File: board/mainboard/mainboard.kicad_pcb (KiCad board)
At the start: 2 copper layers, 148.1 x 58.4 mm, 97 parts, among them P1 I2C, P10 BUMPERS, P12 POWER, P2 MOTOR 1, P3 MOTOR 2, P4 SPI, P5 DAC, P6 LINE SENSORS, P7 ANALOG, P8 OPTIONAL PERIPHERALS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

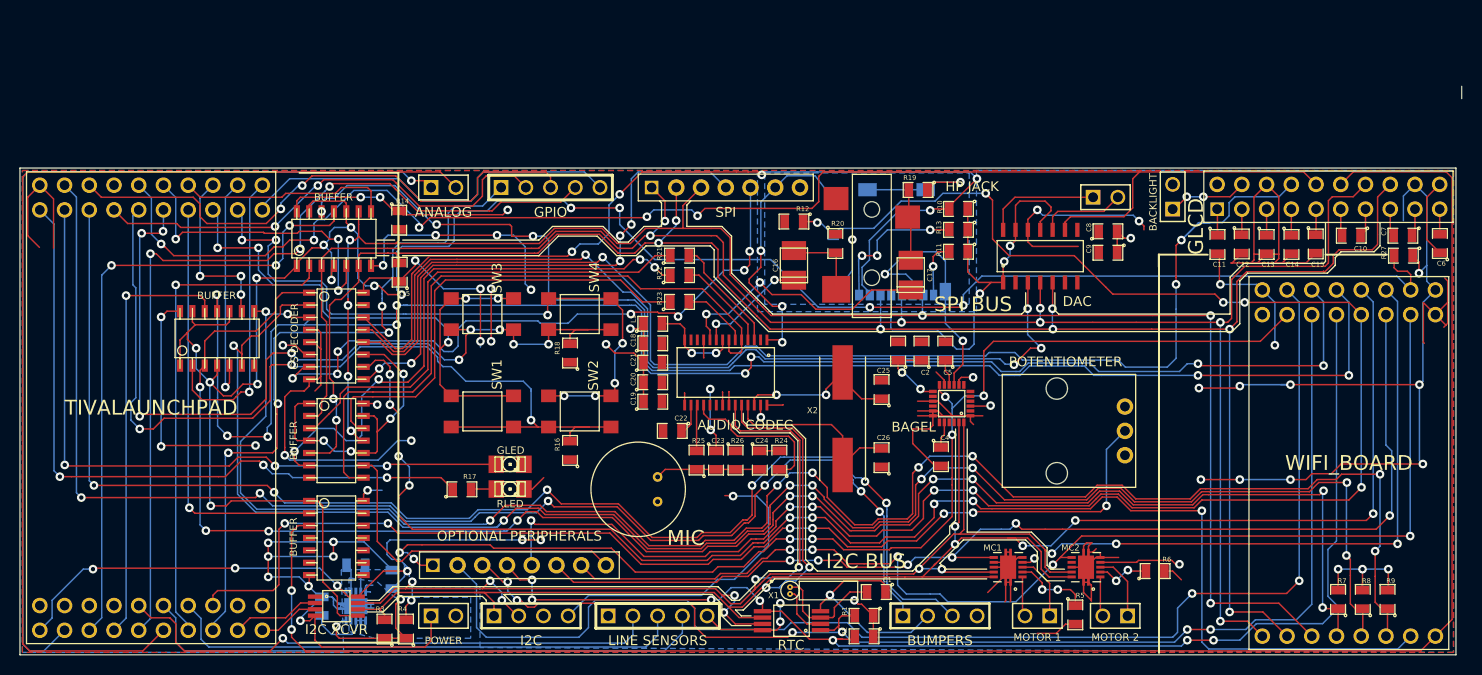
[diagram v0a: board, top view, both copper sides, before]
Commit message: Fixed busses to be same width
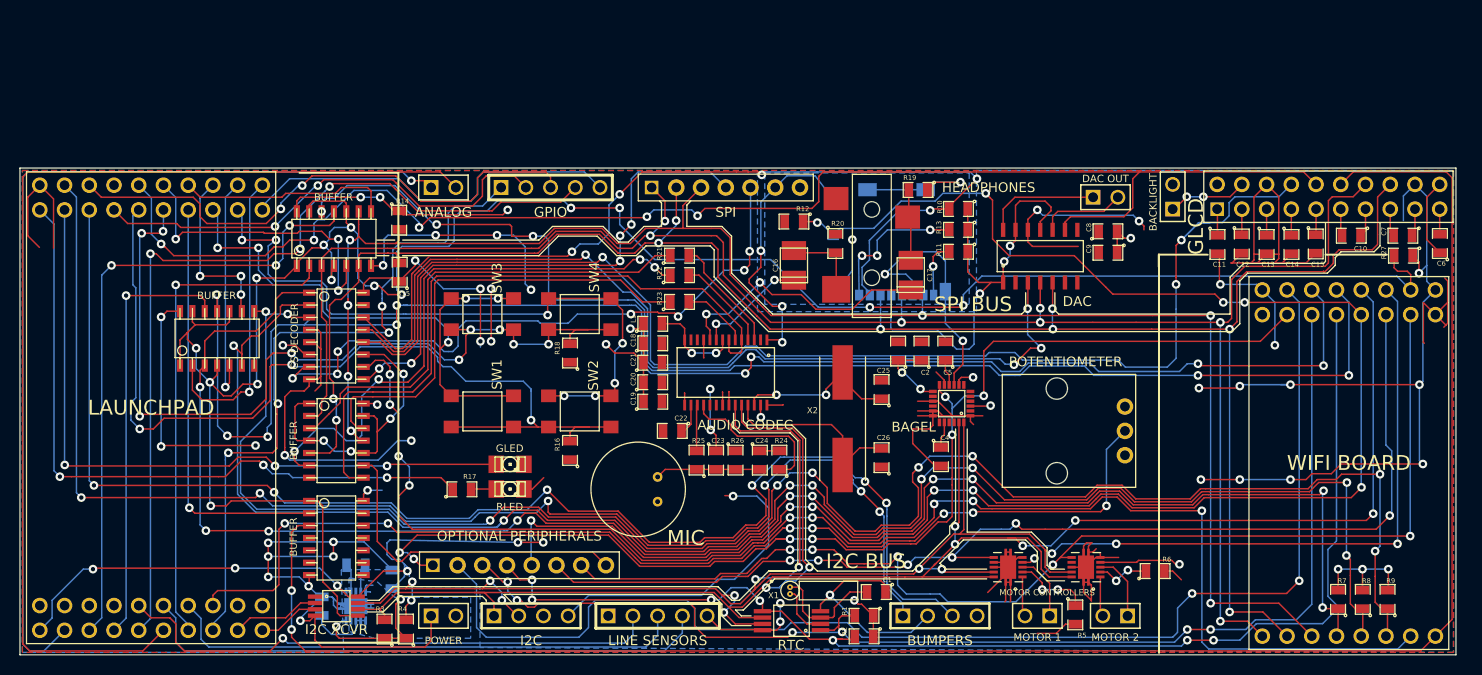
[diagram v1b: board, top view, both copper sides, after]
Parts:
- DAC OUT: renamed from P5
- HP1: value HP JACK -> HEADPHONES
- LP1: value TIVALAUNCHPAD -> LAUNCHPAD
- MOTOR CONTROLLERS: renamed from MC1
- WB1: value WIFI_BOARD -> WIFI BOARD
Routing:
- net BUMP2: track 138.1 -> 140.5 mm
- net BUMP1: track 137.6 -> 139.9 mm
- net SPI_SEL2: track 181.1 -> 183.1 mm
- net MPUINT: track 120.6 -> 122.4 mm
- net SPI_SEL1: track 177.0 -> 178.5 mm
- net SPI_SEL0: track 178.2 -> 179.5 mm
- net SD_SWITCH: track 186.3 -> 187.1 mm
- net POT: track 113.5 -> 114.2 mm
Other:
- board size 148.1 x 58.4 mm -> 147.5 x 50 mm
- board text added: "Proxima Rev 1.1"

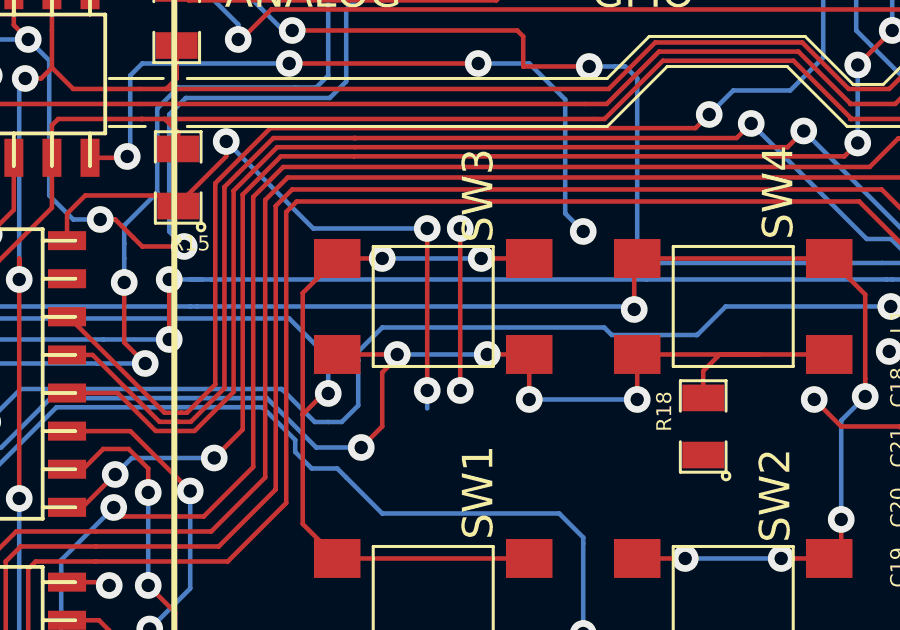
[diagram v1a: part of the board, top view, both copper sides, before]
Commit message: Fixed bug with an unconnected net
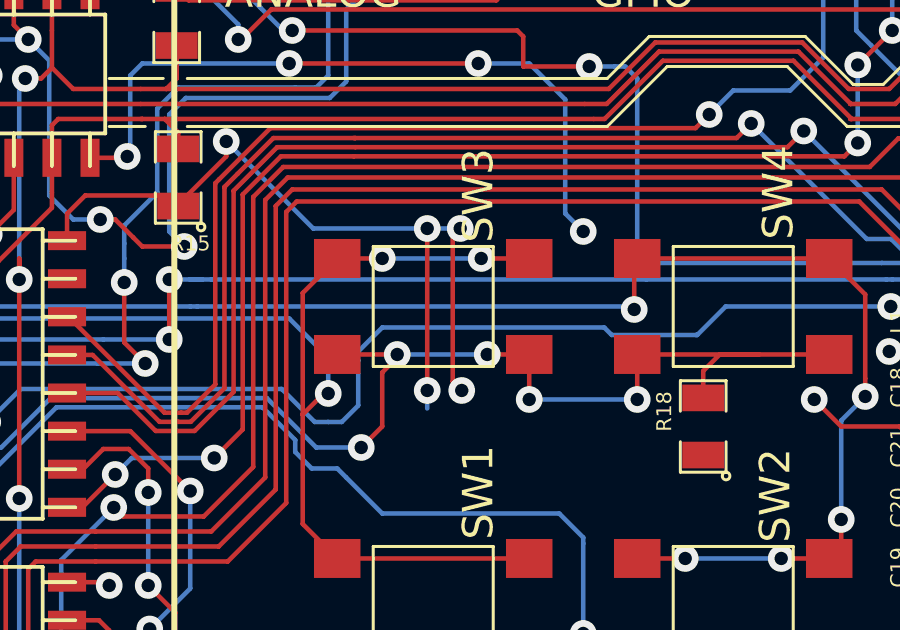
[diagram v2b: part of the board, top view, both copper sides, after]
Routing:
- net 3V3: track 377.8 -> 384.6 mm, vias 48 -> 50
- net (no net): track 5.40 -> 0.00 mm, vias 2 -> 0
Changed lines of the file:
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@@
     (thickness 1.6)
     (drawings 125)
-    (tracks 2750)
+    (tracks 2753)
     (zones 0)
     (modules 97)
@@
   (gr_line (start 156.21 158.75) (end 166.37 158.75) (angle 90) (layer F.SilkS) (width 0.2))
   (gr_line (start 244.475 118.885) (end 244.475 120.155) (angle 90) (layer F.SilkS) (width 0.2))
-  (via (at 175.9 127.8) (size 0.889) (layers F.Cu B.Cu) (net 0))
-  (via (at 175.9 122.4) (size 0.889) (layers F.Cu B.Cu) (net 0))
-  (segment (start 175.9 127.8) (end 175.9 122.4) (width 0.1524) (layer F.Cu) (net 0))
+  (segment (start 174.8 122.4) (end 175.9 122.4) (width 0.1524) (layer B.Cu) (net 1))
+  (via (at 175.95 127.8) (size 0.889) (layers F.Cu B.Cu) (net 1))
+  (segment (start 175.65 127.5) (end 175.95 127.8) (width 0.1524) (layer F.Cu) (net 1))
+  (segment (start 175.65 122.65) (end 175.65 127.5) (width 0.1524) (layer F.Cu) (net 1))
+  (segment (start 175.9 122.4) (end 175.65 122.65) (width 0.1524) (layer F.Cu) (net 1))
+  (via (at 175.9 122.4) (size 0.889) (layers F.Cu B.Cu) (net 1))
   (segment (start 129.54 157.48) (end 130.8 156.22) (width 0.1524) (layer B.Cu) (net 1))
   (segment (start 158.3 151.1) (end 160.1 152.9) (width 0.1524) (layer B.Cu) (net 1))

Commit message: Added Penguin Skywalker
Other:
- board text added: "Proxima Rev 1.1 Penguin Skywalker"
- board text removed: "Proxima Rev 1.1"
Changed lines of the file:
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@@
     (pad_to_mask_clearance 0)
     (aux_axis_origin 0 0)
-    (visible_elements 7FFFFBBF)
+    (visible_elements 7FFFFBAF)
     (pcbplotparams
       (layerselection 284196865)
@@
     )
   )
-  (gr_text "Proxima\nRev 1.1" (at 183.8 137.45) (layer B.SilkS)
-    (effects (font (size 2 2) (thickness 0.3)) (justify mirror))
+  (gr_text "Proxima\nRev 1.1\nPenguin Skywalker" (at 197.4 132.55) (layer B.SilkS)
+    (effects (font (size 2 2) (thickness 0.3)) (justify left mirror))
   )
   (gr_text "SPI BUS" (at 248.8 127.8 90) (layer B.SilkS)

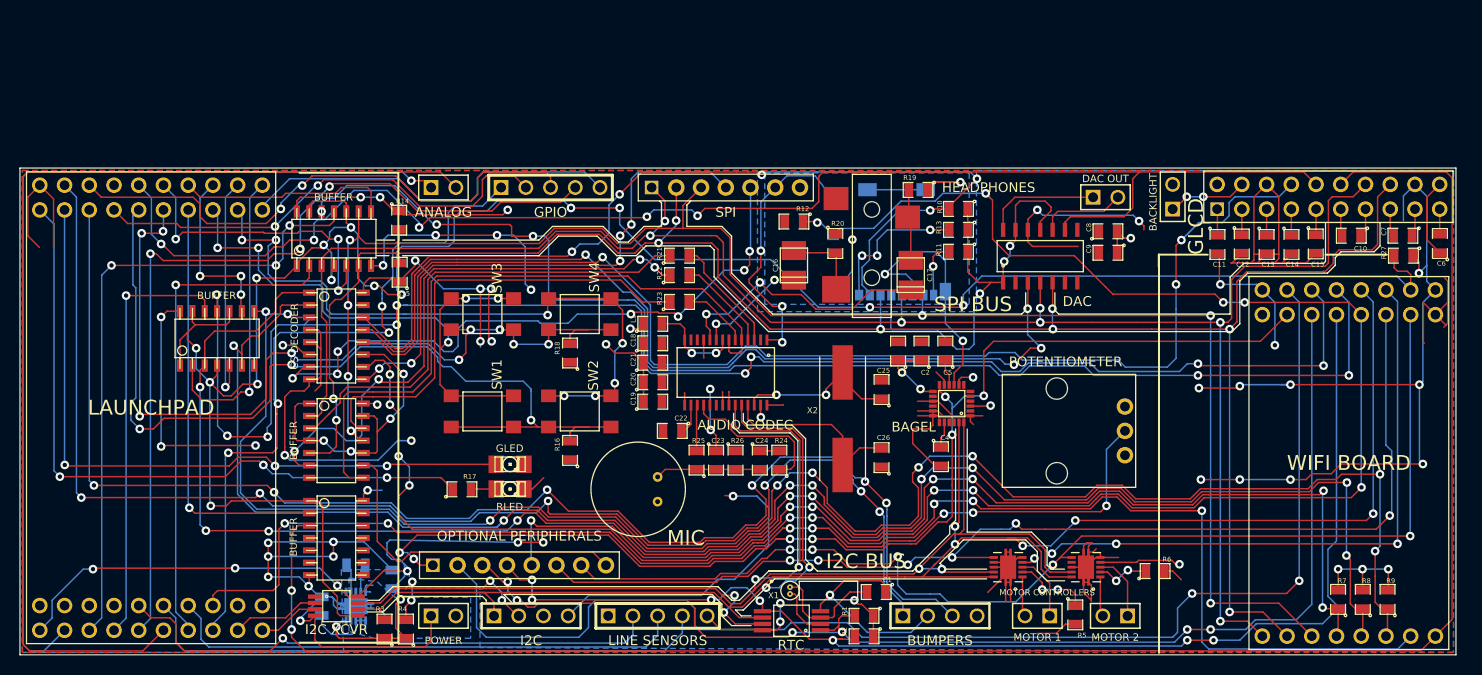
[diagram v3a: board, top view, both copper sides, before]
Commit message: Fixed layout issues with mainboard v1.1
* Increased width of power traces
* Increased number of traces connecting power and ground planes
* Cleaned up some routing
* Reduced via size
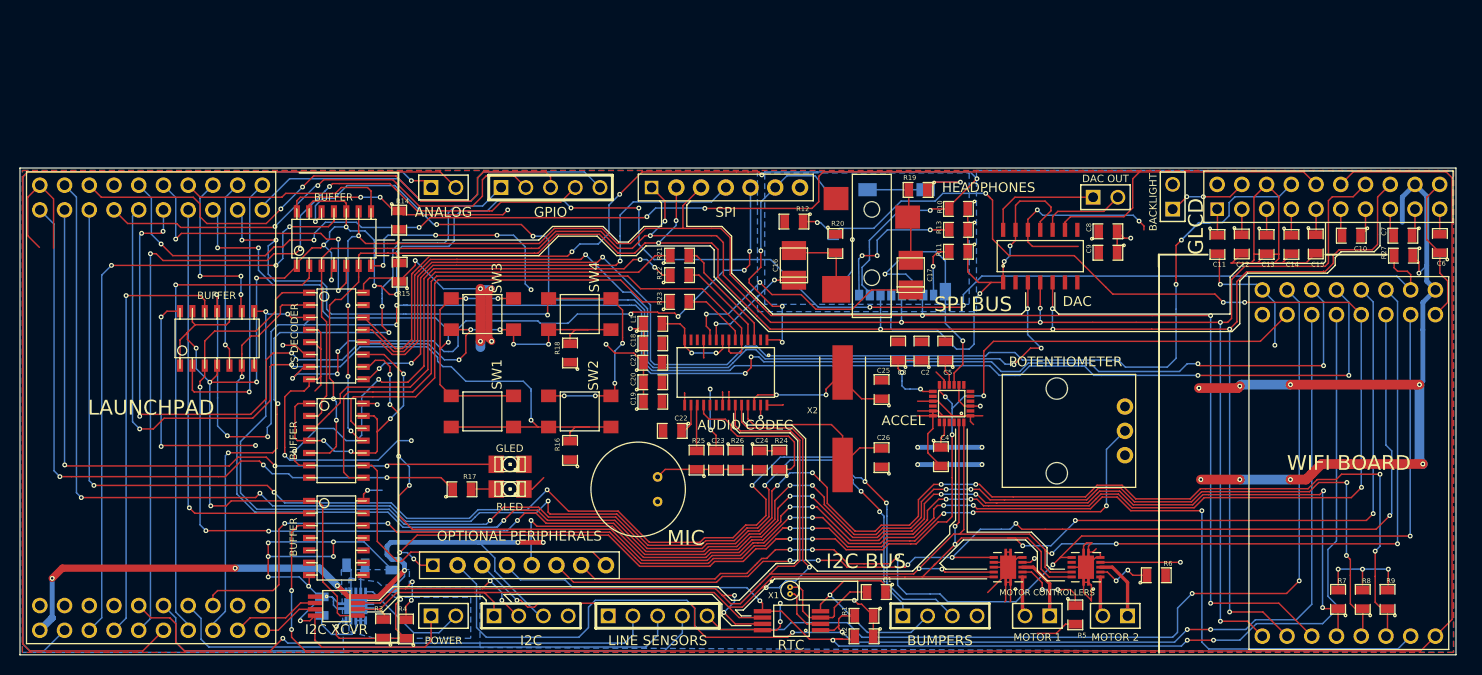
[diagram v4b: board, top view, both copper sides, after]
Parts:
- MPU1: value BAGEL -> ACCEL
- moved R6 0.45 mm to (244.2, 151.8)
- moved R3 0.16 mm to (164.8, 157.3)
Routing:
- net GND: track 430.7 -> 385.5 mm, vias 28 -> 27
- net (no net): track 0.00 -> 13.2 mm, vias 0 -> 4
- net 3V3: track 384.6 -> 395.9 mm, vias 50 -> 49
- net N-00000121: track 10.9 -> 18.8 mm
- net SPI_SEL1: track 178.5 -> 172.2 mm
- net SPI_SEL2: track 183.1 -> 178.2 mm
- net SPI_SEL1_LP: track 23.6 -> 19.2 mm
- net RST: track 149.0 -> 144.9 mm
- net I2C_DA: track 211.0 -> 207.5 mm, vias 13 -> 11
- net SPI_CS6: track 55.6 -> 52.7 mm, vias 5 -> 3
- net RTCINT2: track 127.4 -> 125.1 mm, vias 7 -> 4
- net SPI_SEL0: track 179.5 -> 177.4 mm
- net UART_RX: track 132.8 -> 135.0 mm
- net SD_SWITCH: track 187.1 -> 185.6 mm
- net CC_CONTROL: track 235.8 -> 234.8 mm
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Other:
- net class Default: via_dia 0.889 -> 0.5; via_drill 0.635 -> 0.3
- rule via_min_drill: 0.508 -> 0.3
- rule via_min_size: 0.889 -> 0.5
- board text added: "Crayon Dinosaur RN, DS, HV"
- board text added: "Proxima Rev 1.2"
- board text removed: "Proxima Rev 1.1 Penguin Skywalker"

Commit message: Removed audio codec from layout.
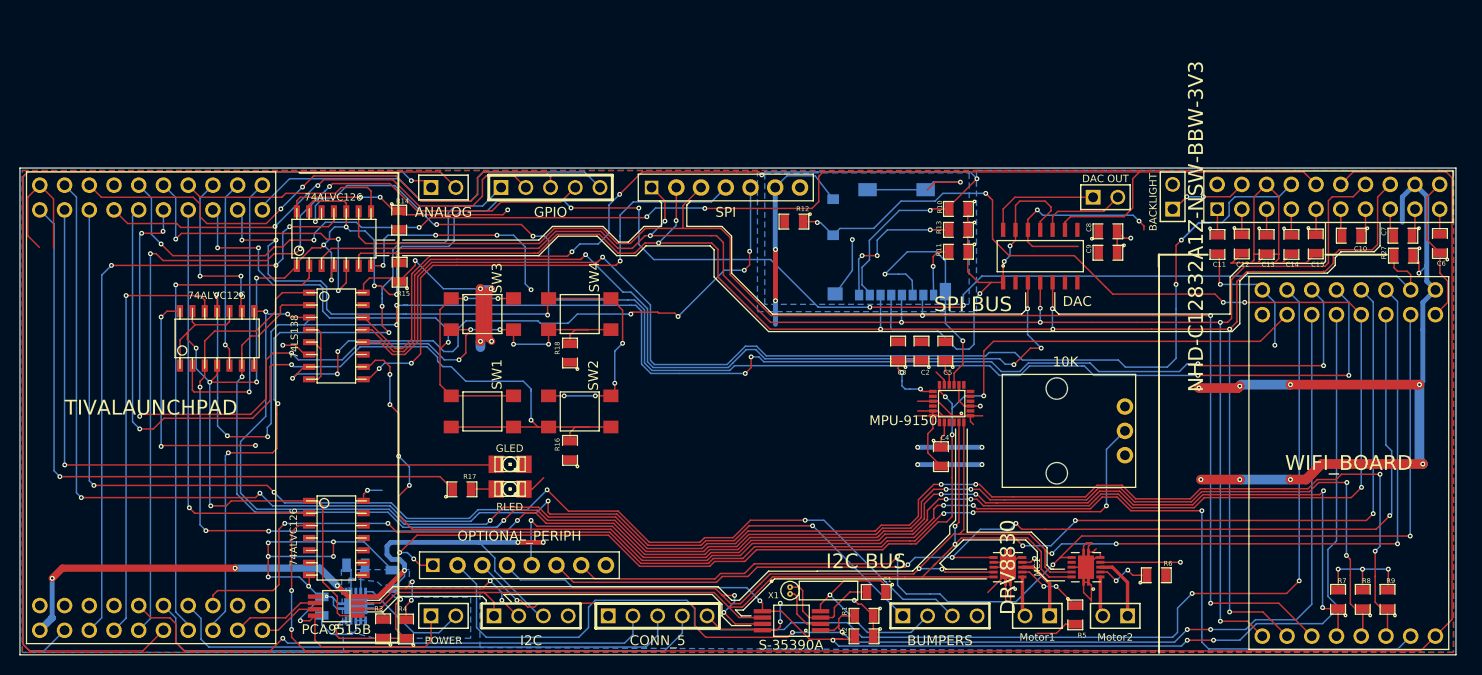
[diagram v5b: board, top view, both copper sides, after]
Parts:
- removed AC1: AUDIO CODEC, WM8731
- removed C16, C17: 330uF, c_tant_B
- removed C18, C20: 0.1uF, SM0805
- removed C19, C21, C22: 10uF, SM0805
- removed C23, C24: 1nF, SM0805
- removed C25, C26: 22pF, SM0805
- removed HP1: HEADPHONES, HeadphoneJack
- removed L1: 10uH, SM0805
- removed MIC1: MIC, CMA-4544
- removed MOTOR CONTROLLERS: DRV8830, DRV8830
- removed R19, R20, R26: 47K, SM0805
- removed R21, R23: 27, SM0805
- removed R22: 1K, SM0805
- removed R24: 330, SM0805
- removed R25: 680, SM0805
- removed U2: BUFFER, so-14
- removed X2: 12.288MHz, HC-49US
- added MC1: DRV8830, DRV8830, F.Cu at (229.0, 151.0)
- GLCD1: value GLCD -> NHD-C12832A1Z-NSW-BBW-3V3
- LP1: value LAUNCHPAD -> TIVALAUNCHPAD
- MPU1: value ACCEL -> MPU-9150
- P2: value MOTOR 1 -> Motor1
- P3: value MOTOR 2 -> Motor2
- P6: value LINE SENSORS -> CONN_5
- P8: value OPTIONAL PERIPHERALS -> OPTIONAL_PERIPH
- REG1: value POWER REG -> TPS63001
- RTC1: value RTC -> S-35390A
- RV1: value POTENTIOMETER -> 10K
- SD1: value SDCARD -> SDCARD_PUSH
- U1: value CS DECODER -> 74LS138
- U3, U4, U5: value BUFFER -> 74ALVC126
- U6: value I2C XCVR -> PCA9515B
- WB1: value WIFI BOARD -> WIFI_BOARD
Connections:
- P8 pad 8: AUD_DAC_CL -> (no net)
- U1 pad 11: SPI_CS4 -> (no net)
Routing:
- net N-00000109: track 68.8 -> 0.00 mm
- net N-00000100: track 59.0 -> 0.00 mm, vias 4 -> 0
- net N-0000097 (its old number): track 50.4 -> 0.00 mm
- net N-00000110: track 48.3 -> 0.00 mm
- net GND: track 385.5 -> 345.9 mm, vias 27 -> 23
- net AUD_DAC_CL: track 34.2 -> 0.00 mm
- net SPI_CS4: track 30.9 -> 0.00 mm, vias 4 -> 0
- net I2C_CL: track 201.5 -> 172.6 mm, vias 7 -> 5
- net N-0000096: track 27.1 -> 0.00 mm, vias 2 -> 0
- net I2C_DA: track 207.5 -> 182.1 mm
- net 3V3: track 395.9 -> 372.4 mm, vias 49 -> 44
- net SPI_MOSI: track 202.3 -> 178.8 mm, vias 9 -> 7
- net SPI_MISO: track 171.3 -> 148.3 mm, vias 7 -> 3
- net N-00000112: track 19.6 -> 0.00 mm
- net SPI_SCK: track 193.7 -> 176.8 mm
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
